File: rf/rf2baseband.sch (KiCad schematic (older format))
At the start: 30 parts, among them U601 TLV4172

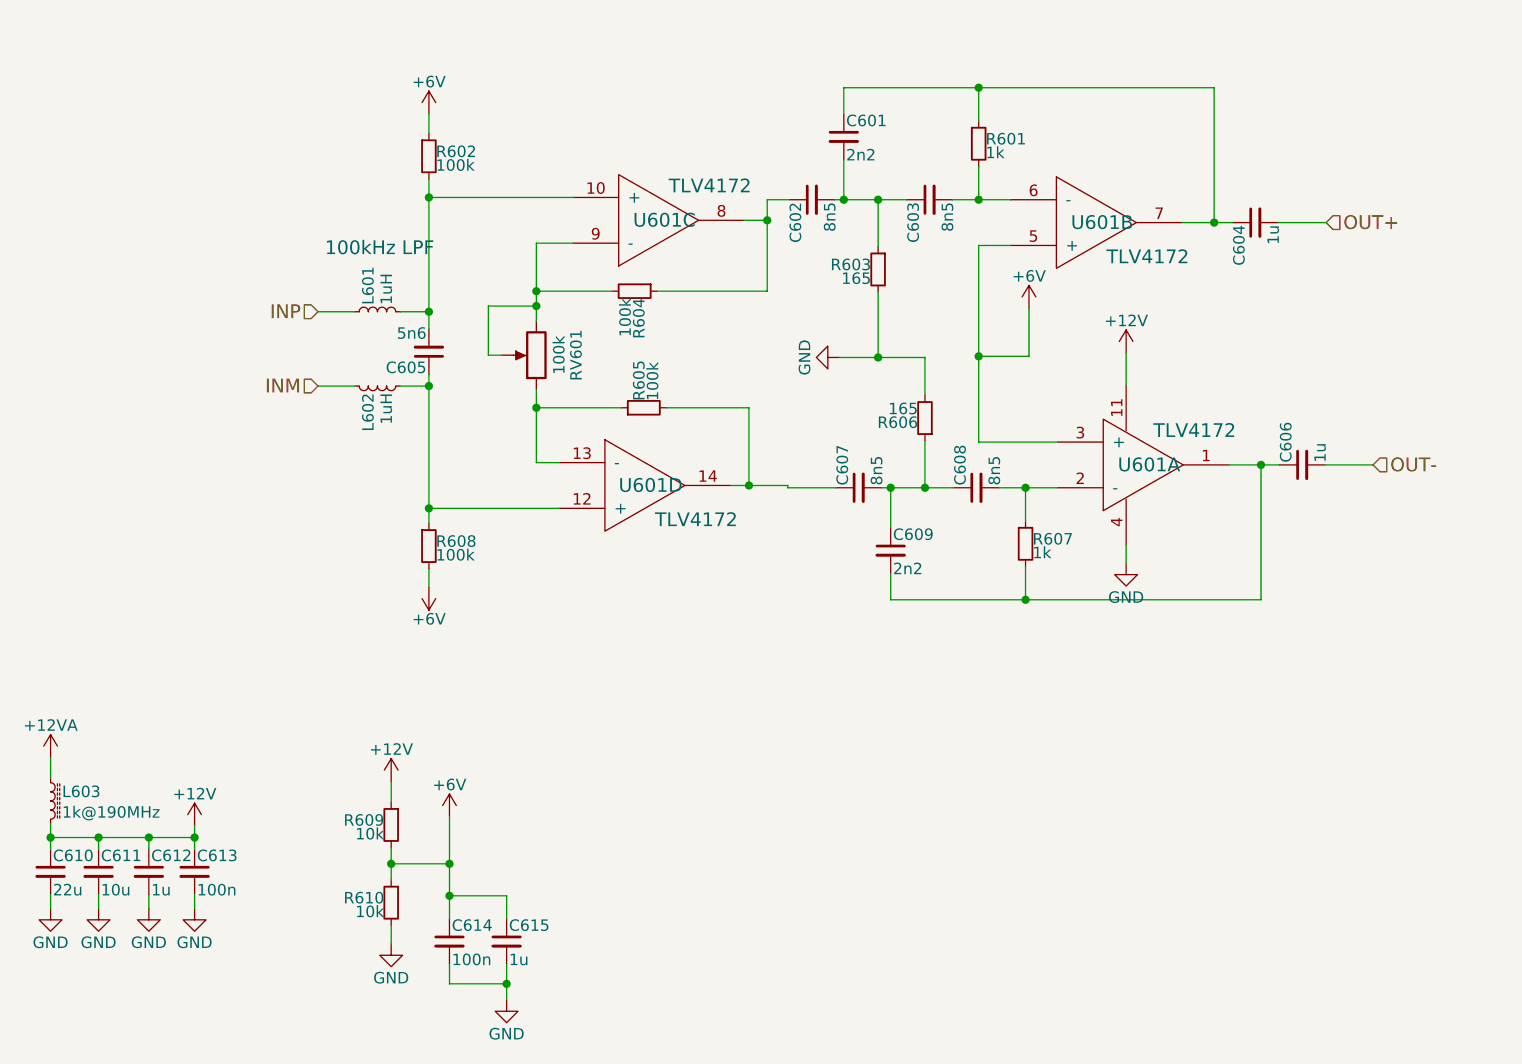
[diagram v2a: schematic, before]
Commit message: Convert high pass from MFB to Sallen-Key; forgot about low input impedance for high pass MFB
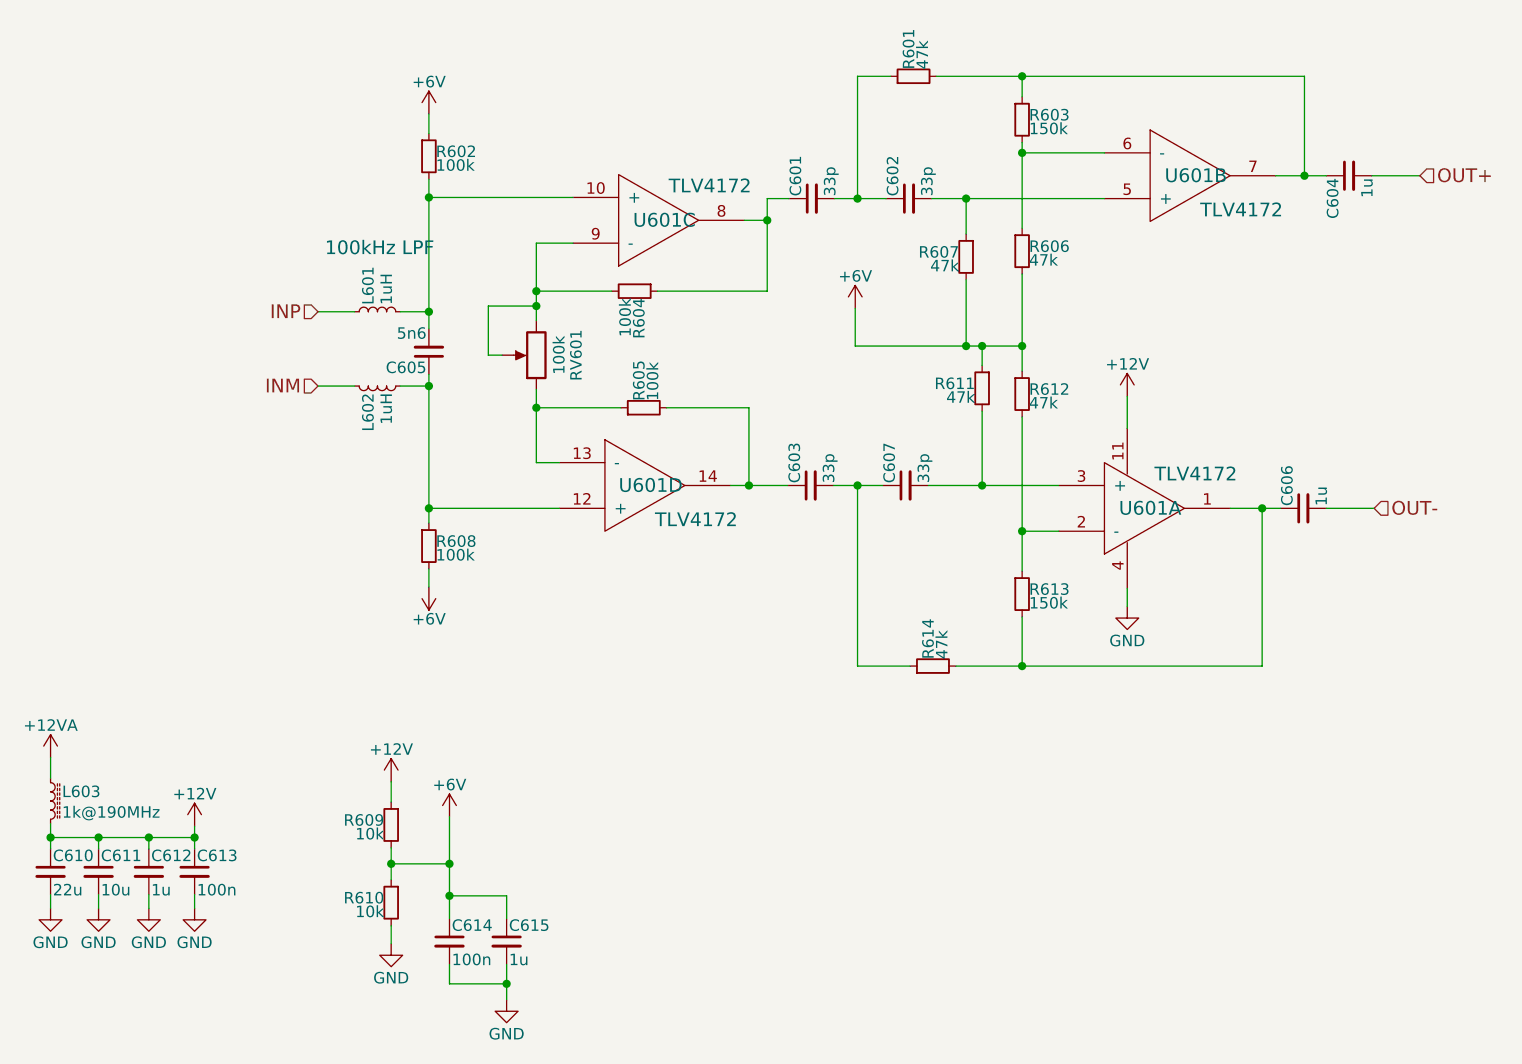
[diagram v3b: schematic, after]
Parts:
- removed C608: 8n5, Capacitors_SMD:C_0603_HandSoldering, symbol C_Small
- removed C609: 2n2, Capacitors_SMD:C_0603_HandSoldering, symbol C_Small
- added R611, R612, R614: 47k, Resistors_SMD:R_0603_HandSoldering, symbol R_Small
- added R613: 150k, Resistors_SMD:R_0402, symbol R_Small
- C601: value 2n2 -> 33p
- C602, C603, C607: value 8n5 -> 33p
- R601, R607: value 1k -> 47k; footprint Resistors_SMD:R_1206_HandSoldering -> Resistors_SMD:R_0603_HandSoldering
- R603: value 165 -> 150k; footprint Resistors_SMD:R_1206_HandSoldering -> Resistors_SMD:R_0402
- R606: value 165 -> 47k; footprint Resistors_SMD:R_1206_HandSoldering -> Resistors_SMD:R_0603_HandSoldering
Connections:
- net +6V: now also R606.2, R607.2, R611.1, R612.1; no longer U601.3 (+), U601.5 (+)
- net GND: no longer R603.2, R606.2
- net at R605.2, U601.14: now also C603.1; no longer C607.1
- net at C606.1, U601.1: now also R613.2, R614.2; no longer R607.2
- net at U601.2 (-): now also R612.2, R613.1; no longer R607.1
- net at C604.1, U601.7: now also R601.2, R603.1; no longer C601.1, R601.1
- net at R604.1, U601.8: now also C601.1; no longer C602.1
- net at C607.2: now also U601.3 (+), R611.2; no longer R606.1
- new net: C602.2, R607.1, U601.5 (+)
- new net: R603.2, R606.1, U601.6 (-)
- new net: C601.2, C602.1, R601.1
- new net: C603.2, C607.1, R614.1
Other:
- moved on the sheet: C604, C606, U601A, U601B

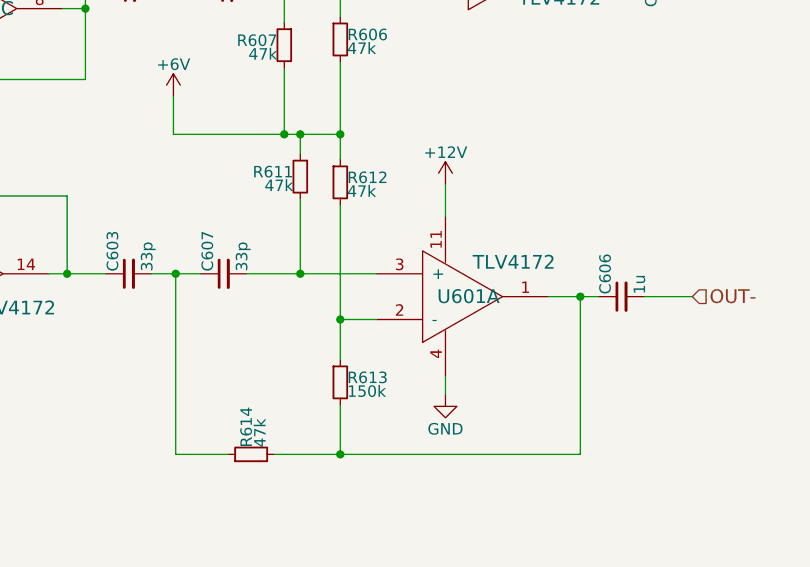
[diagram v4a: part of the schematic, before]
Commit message: Fix voltage rails on op amp
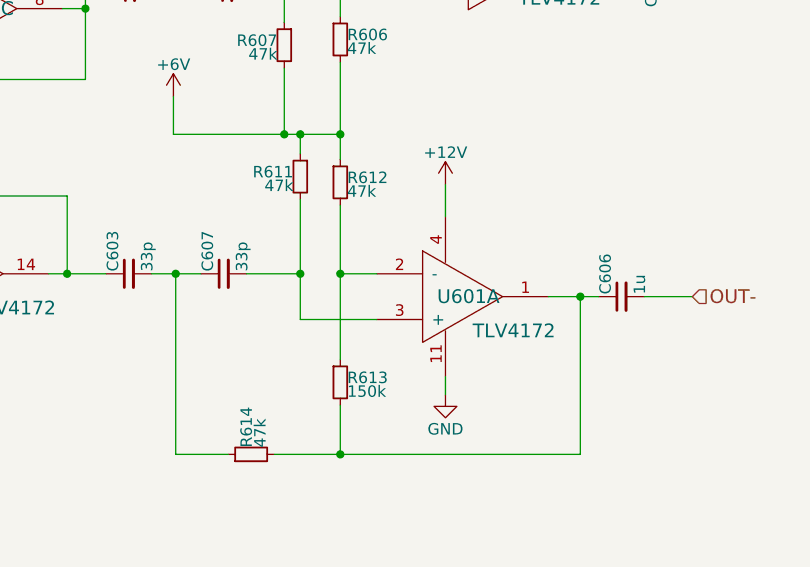
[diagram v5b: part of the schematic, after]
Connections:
- net +12V: now also U601.4; no longer U601.11
- net GND: now also U601.11; no longer U601.4
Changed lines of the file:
@@
 F 3 "" H 5805 3385 60  0001 C CNN
 	1    5805 3385
-	1    0    0    1
+	1    0    0    -1
 $EndComp
 $Comp
@@
 	5070 2675 5070 2760
 Wire Wire Line
-	5070 2960 5070 3285
-Wire Wire Line
-	4835 3285 5405 3285
-Connection ~ 5070 3285
+	5070 2960 5070 3485
 Wire Wire Line
 	5245 2985 5245 3660
-Wire Wire Line
-	5245 3485 5405 3485
-Connection ~ 5245 3485
 Wire Wire Line
 	5245 3860 5245 4075
@@
 Connection ~ 5245 2675
 Connection ~ 5070 2675
+Wire Wire Line
+	5070 3485 5405 3485
+Wire Wire Line
+	4835 3285 5070 3285
+Connection ~ 5070 3285
+Wire Wire Line
+	5405 3285 5245 3285
+Connection ~ 5245 3285
 $EndSCHEMATC
